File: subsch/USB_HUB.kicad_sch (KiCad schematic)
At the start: 7 parts

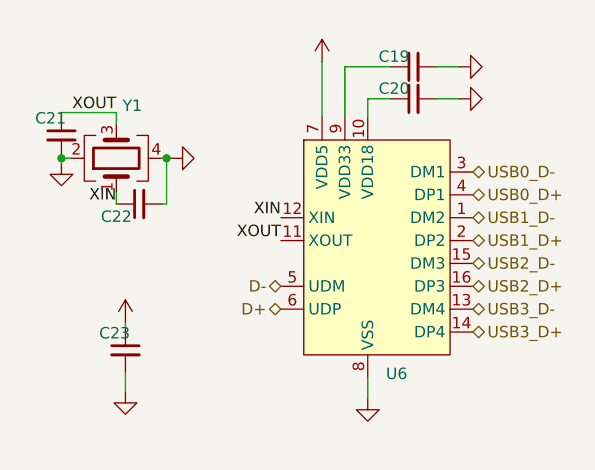
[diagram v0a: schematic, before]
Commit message: Big update on UART-pilot lamp/routings/connectors/esd protection
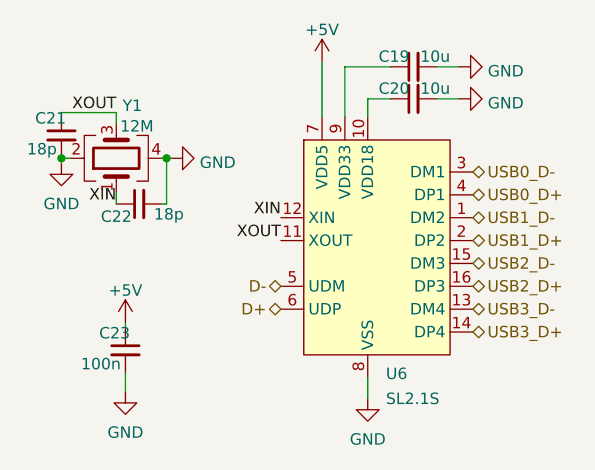
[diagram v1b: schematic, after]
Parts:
- C19, C20: value (none) -> 10u; footprint (none) -> Capacitor_SMD:C_0603_1608Metric
- C21, C22: value (none) -> 18p; footprint (none) -> Capacitor_SMD:C_0603_1608Metric
- C23: value (none) -> 100n; footprint (none) -> Capacitor_SMD:C_0603_1608Metric
- U6: value (none) -> SL2.1S; footprint (none) -> MyLib:SL2.1S-SSOP-16
- Y1: value (none) -> 12M; footprint (none) -> Crystal:Crystal_SMD_3225-4Pin_3.2x2.5mm
